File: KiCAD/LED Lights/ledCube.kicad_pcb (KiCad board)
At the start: 2 copper layers, 52 x 22 mm, 14 parts, among them P1 CONN_01X03, P2 CONN_01X02, P3 CONN_01X02, P4 CONN_01X02, P5 CONN_01X02, U1 AL8805W5

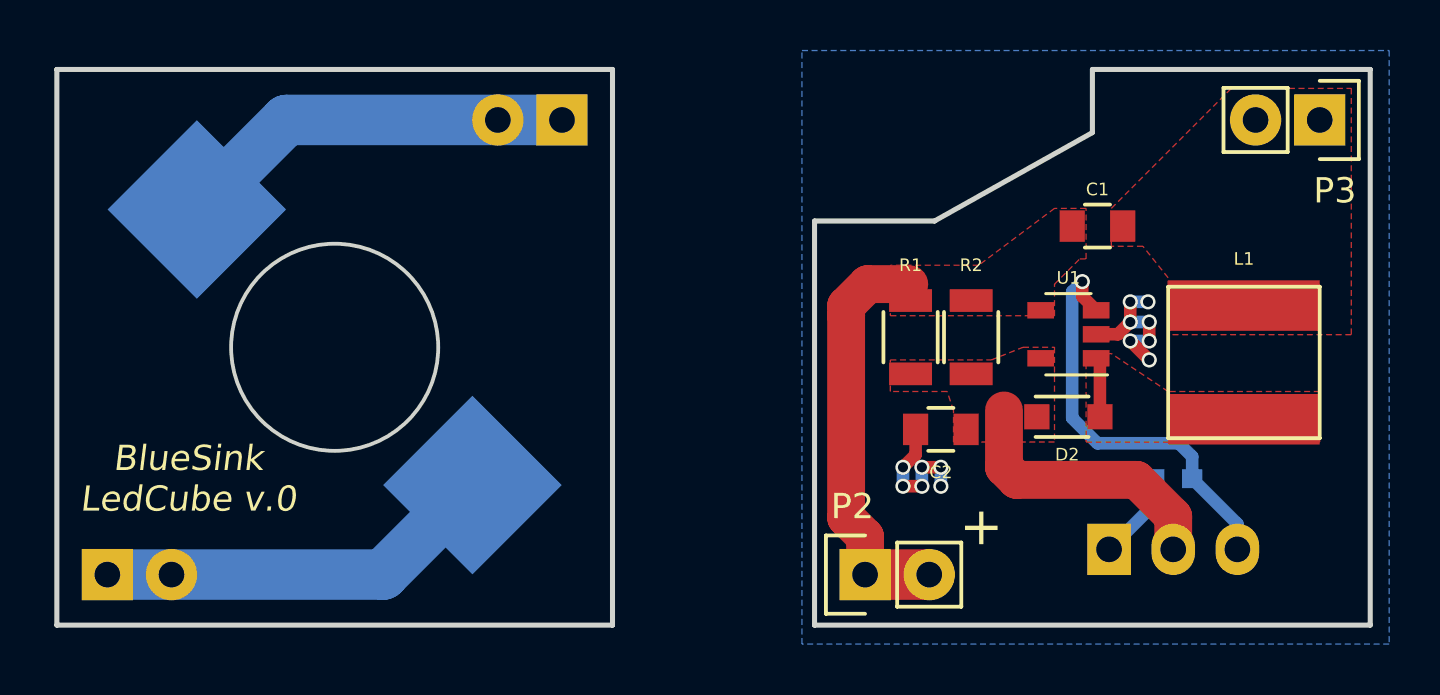
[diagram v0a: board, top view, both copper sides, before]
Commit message: updated LED Cube to latest kicad
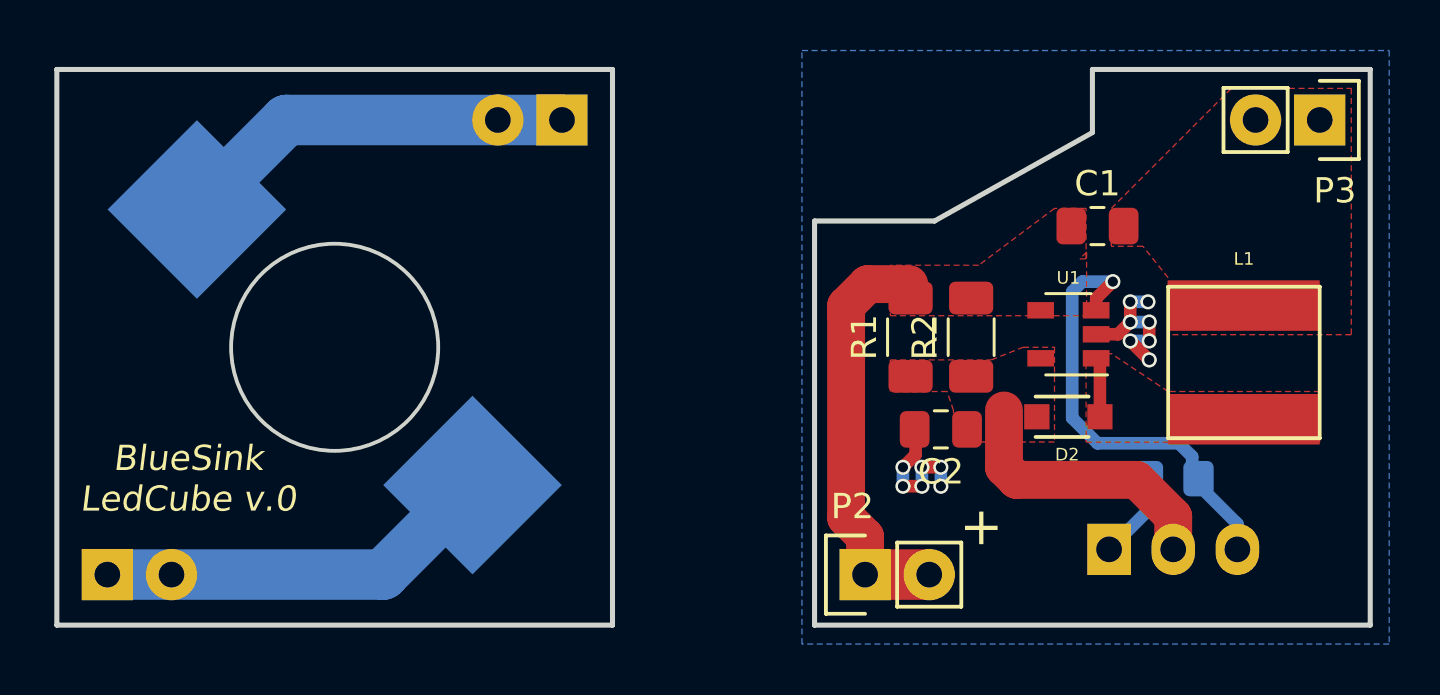
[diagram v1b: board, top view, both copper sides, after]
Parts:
- C1, C2: footprint Capacitors_SMD:C_0805 -> Capacitor_SMD:C_0805_2012Metric_Pad1.18x1.45mm_HandSolder
- R1, R2: footprint Resistors_SMD:R_1206 -> Resistor_SMD:R_1206_3216Metric_Pad1.30x1.75mm_HandSolder
- R3: footprint Capacitors_SMD:C_0603 -> Resistor_SMD:R_0805_2012Metric_Pad1.20x1.40mm_HandSolder
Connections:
- net /LED+/L renamed /LED+/L
- net /LED+/U renamed /LED+/U
- net /LED-/L renamed /LED-/L
- net /LED-/U renamed /LED-/U
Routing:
- net /PWM: track 16.9 -> 18.1 mm
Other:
- net class Default removed
